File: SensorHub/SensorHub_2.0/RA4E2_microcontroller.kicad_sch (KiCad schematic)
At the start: 29 parts, among them J5 FTSH-105-01-L-DV-K-A, SW1 SW_Push, SW2 SW_Push, U1 R7FA4E2B93CFM#AA0, Y1 ASH7KW-32.768KHZ-L-T

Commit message: Fix2 17.04
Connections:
- no-connect marks 36 -> 38
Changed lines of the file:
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@@
+	)
+	(no_connect
+		(at 246.38 118.11)
 	)
 	(no_connect
@@
 	)
 	(no_connect
+		(at 246.38 115.57)
+	)
+	(no_connect

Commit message: Vesrion 2
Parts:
- removed J5: FTSH-105-01-L-DV-K-A, FTSH-105-01-L-DV-K-A:SAMTEC_FTSH-105-01-L-DV-K-A, symbol FTSH-105-01-L-DV-K-A:FTSH-105-01-L-DV-K-A
- removed R5: 1.5 K, Resistor_SMD:R_0201_0603Metric, symbol Device:R
- removed R6: 10 K, Resistor_SMD:R_0201_0603Metric, symbol Device:R
- removed SW2: SW_Push, Library:B3U-1000P(M)-B, symbol Library:SW_Push
- added J1: Conn_01x04_Pin, Connector_PinHeader_1.27mm:PinHeader_1x04_P1.27mm_Vertical, symbol Connector:Conn_01x04_Pin
- added U9: USBLC6-4SC6, Package_TO_SOT_SMD:SOT-23-6, symbol Power_Protection:USBLC6-4SC6
- TP1, TP10, TP3, TP4, TP5, TP6, TP8: footprint TestPoint:TestPoint_THTPad_D1.0mm_Drill0.5mm -> TestPoint:TestPoint_Pad_1.0x1.0mm
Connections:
- net +3.3V: now also J1.4 (Pin_4), U9.5 (VBUS)
- net GND: now also J1.3 (Pin_3), U9.2 (GND)
- net GP1: now also U1.49 (CACREF); no longer U1.14 (P409)
- net GP2: now also U1.22 (P206); no longer U1.30 (P302)
- net GP3: now also U1.21 (CACREF); no longer U1.29 (P303)
- net INT1: now also U1.51 (P006); no longer U1.1 (P400)
- net INT2: now also U1.50 (P008); no longer U1.44 (P104)
- net LED: now also U1.54 (P013); no longer U1.27 (P200)
- net RXD: now also TP8.1, U1.3 (CACREF); no longer U1.48 (P100)
- net SCL_0: now also U1.48 (P100); no longer U1.2 (P401)
- net SDA_0: now also U1.47 (P101); no longer U1.4 (P403)
- net SWCLK: now also J1.1 (Pin_1), U9.1 (I/O1)
- net SWDIO: now also J1.2 (Pin_2), U9.3 (I/O2)
- net TXD: now also U1.2 (P401); no longer TP8.1, U1.47 (P101)
- no-connect marks 38 -> 35
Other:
- note added: "Reset"
- note removed: "Reset/Boot"
- moved on the sheet: C7, R4, SW1

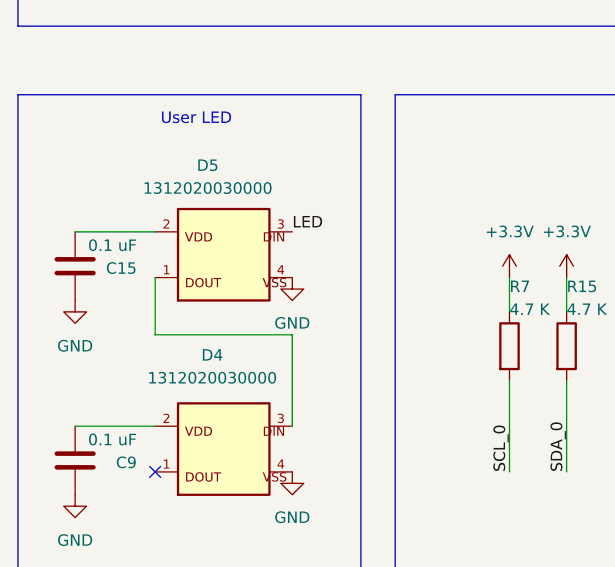
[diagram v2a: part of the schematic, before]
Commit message: MPN + CC fix
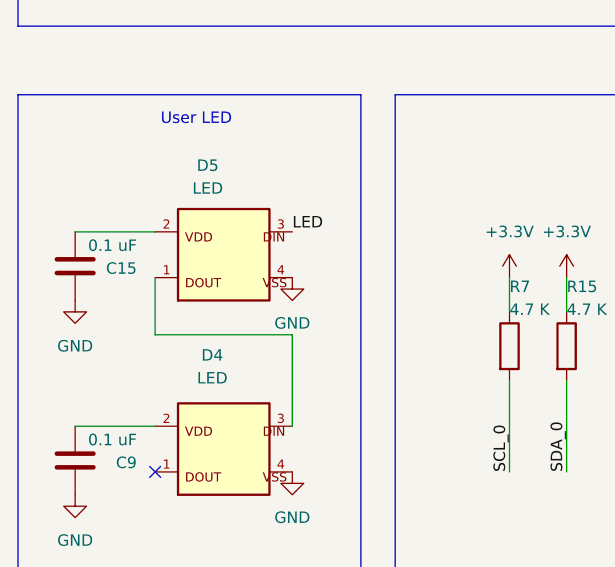
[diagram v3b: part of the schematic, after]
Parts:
- D4, D5: value 1312020030000 -> LED; MPN (none) -> 1312020030000
- SW1: MPN (none) -> B3U-1000PM-B
- U1: MPN (none) -> R7FA4E2B93CFM#AA0
- U9: MPN (none) -> USBLC6-4SC6Y
- Y1: MPN (none) -> ASH7KW-32.768KHZ-L-T
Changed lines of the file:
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@@
 			)
 		)
-		(property "Datasheet" ""
+		(property "Datasheet" "https://nl.mouser.com/datasheet/3/184/1/ASH7KW.pdf"
 			(at 54.61 93.98 0)
 			(effects
@@
 				)
 				(justify bottom)
+				(hide yes)
+			)
+		)
+		(property "MPN" "ASH7KW-32.768KHZ-L-T "
+			(at 54.61 93.98 0)
+			(effects
+				(font
+					(size 1.27 1.27)
+				)
 				(hide yes)
 			)
@@
 			)
 		)
+		(property "MPN" "R7FA4E2B93CFM#AA0"
+			(at 203.2 36.83 0)
+			(effects
+				(font
+					(size 1.27 1.27)
+				)
+				(hide yes)
+			)
+		)
 		(pin "39"
 		)
@@
 			)
 		)
-		(property "Value" "1312020030000"
+		(property "Value" "LED"
 			(at 45.212 125.984 0)
 			(effects
@@
 			)
 		)
-		(property "Datasheet" ""
+		(property "Datasheet" "https://www.we-online.com/components/products/datasheet/1312020030000.pdf"
 			(at 46.99 133.35 0)
 			(effects
@@
 				)
 				(justify bottom)
+				(hide yes)
+			)
+		)
+		(property "MPN" "1312020030000"
+			(at 46.99 133.35 0)
+			(effects
+				(font
+					(size 1.27 1.27)
+				)
 				(hide yes)
 			)
@@
 			)
 		)
-		(property "Datasheet" "~"
+		(property "Datasheet" "https://www.mouser.com/catalog/specsheets/en-b3u.pdf?_gl=1*1hale0w*_gcl_aw*R0NMLjE3Nzc1NDczODcuQ2p3S0NBanctOHZQQmhCYkVpd0FvQTM5V21qOE1FMEhGMTJsZnVsd1dsanpUT2lLOUp5a3NWMndHOXk0X2pxV0NTQ1ZHQTdyREplemFSb0NiajRRQXZEX0J3RQ..*_gcl_au*MTEyMDA2MzkwNS4xNzczNDExMzc2LjMyODU5NDQyNi4xNzc3NTQ2NjQ1LjE3Nzc1NDg3NTQ.*_ga*Mjg1MTQ4MTY2LjE3NzM0MTEzNzc.*_ga_15W4STQT4T*czE3Nzc1NDUwNzgkbzU0JGcxJHQxNzc3NTQ4NzU4JGozJGwwJGgw"
 			(at 139.7 57.15 0)
 			(effects
@@
 		(property "Description" "Push button switch, generic, two pins"
 			(at 144.78 57.15 0)
+			(effects
+				(font
+					(size 1.27 1.27)
+				)
+				(hide yes)
+			)
+		)
+		(property "MPN" "B3U-1000PM-B"
+			(at 144.78 57.15 90)
 			(effects
 				(font
@@
 			)
 		)
+		(property "MPN" "USBLC6-4SC6Y "
+			(at 82.55 50.8 0)
+			(effects
+				(font
+					(size 1.27 1.27)
+				)
+				(hide yes)
+			)
+		)
 		(pin "6"
 		)
@@
 			)
 		)
-		(property "Value" "1312020030000"
+		(property "Value" "LED"
 			(at 45.72 147.066 0)
 			(effects
@@
 			)
 		)
-		(property "Datasheet" ""
+		(property "Datasheet" "https://www.we-online.com/components/products/datasheet/1312020030000.pdf"
 			(at 46.99 154.94 0)
 			(effects
@@
 				(hide yes)
 			)
+		)
+		(property "MPN" "1312020030000"
+			(at 46.99 154.94 0)
+			(effects
+				(font
+					(size 1.27 1.27)
+				)
+				(hide yes)
+			)

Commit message: pcb fix
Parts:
- added R17, R18: 4.7 K, Resistor_SMD:R_0402_1005Metric, symbol Device:R
- R15, R4, R7: footprint Resistor_SMD:R_0201_0603Metric -> Resistor_SMD:R_0402_1005Metric
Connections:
- net USB_DM: now also R18.2; no longer U1.18 (USB_DM)
- net USB_DP: now also R17.2; no longer U1.19 (USB_DP)
- new net DM: R18.1, U1.18 (USB_DM)
- new net DP: R17.1, U1.19 (USB_DP)
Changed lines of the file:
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@@
 	)
 	(rectangle
+		(start 114.3 148.59)
+		(end 137.16 189.23)
+		(stroke
+			(width 0)
+			(type default)
+		)
+		(fill
+			(type none)
+		)
+	)
+	(rectangle
 		(start 66.04 115.57)
 		(end 97.79 170.18)
@@
 	(wire
 		(pts
+			(xy 121.92 177.8) (xy 121.92 171.45)
+		)
+		(stroke
+			(width 0)
+			(type default)
+		)
+	)
+	(wire
+		(pts
 			(xy 137.16 66.04) (xy 144.78 66.04)
 		)
@@
 	(wire
 		(pts
+			(xy 128.27 163.83) (xy 128.27 156.21)
+		)
+		(stroke
+			(width 0)
+			(type default)
+		)
+	)
+	(wire
+		(pts
 			(xy 138.43 123.19) (xy 138.43 115.57)
 		)
@@
 	(wire
 		(pts
+			(xy 128.27 177.8) (xy 128.27 171.45)
+		)
+		(stroke
+			(width 0)
+			(type default)
+		)
+	)
+	(wire
+		(pts
 			(xy 133.35 49.53) (xy 137.16 49.53)
 		)
@@
 	(wire
 		(pts
+			(xy 121.92 156.21) (xy 121.92 163.83)
+		)
+		(stroke
+			(width 0)
+			(type default)
+		)
+	)
+	(wire
+		(pts
 			(xy 161.29 115.57) (xy 161.29 123.19)
 		)
@@
 		)
 	)
+	(label "DM"
+		(at 205.74 87.63 180)
+		(effects
+			(font
+				(size 1.27 1.27)
+			)
+			(justify right bottom)
+		)
+	)
 	(label "+3.3V"
 		(at 153.67 99.06 180)
@@
 		)
 	)
+	(label "DP"
+		(at 205.74 85.09 180)
+		(effects
+			(font
+				(size 1.27 1.27)
+			)
+			(justify right bottom)
+		)
+	)
 	(label "SWCLK"
 		(at 205.74 95.25 180)
@@
 		)
 	)
+	(label "DP"
+		(at 121.92 156.21 90)
+		(effects
+			(font
+				(size 1.27 1.27)
+			)
+			(justify left bottom)
+		)
+	)
 	(label "SWCLK"
 		(at 60.96 49.53 0)
@@
 		)
 	)
+	(label "DM"
+		(at 128.27 156.21 90)
+		(effects
+			(font
+				(size 1.27 1.27)
+			)
+			(justify left bottom)
+		)
+	)
 	(hierarchical_label "MOSI"
 		(shape input)
@@
 		)
 	)
+	(hierarchical_label "USB_DP"
+		(shape input)
+		(at 121.92 177.8 270)
+		(effects
+			(font
+				(size 1.27 1.27)
+			)
+			(justify right)
+		)
+	)
 	(hierarchical_label "SCK"
 		(shape input)
@@
 		)
 	)
-	(hierarchical_label "SDA_0"
+	(hierarchical_label "USB_DM"
 		(shape input)
-		(at 246.38 46.99 0)
+		(at 128.27 177.8 270)
 		(effects
 			(font
 				(size 1.27 1.27)
 			)
-			(justify left)
+			(justify right)
 		)
 	)
-	(hierarchical_label "INT1"
+	(hierarchical_label "SDA_0"
 		(shape input)
-		(at 205.74 130.81 180)
+		(at 246.38 46.99 0)
 		(effects
 			(font
 				(size 1.27 1.27)
 			)
-			(justify right)
+			(justify left)
 		)
 	)
-	(hierarchical_label "USB_DP"
+	(hierarchical_label "INT1"
 		(shape input)
-		(at 205.74 85.09 180)
+		(at 205.74 130.81 180)
 		(effects
 			(font
@@
 		)
 	)
-	(hierarchical_label "USB_DM"
-		(shape input)
-		(at 205.74 87.63 180)
-		(effects
-			(font
-				(size 1.27 1.27)
-			)
-			(justify right)
-		)
-	)
 	(hierarchical_label "RXD"
 		(shape input)
@@
 			)
 		)
-		(property "Footprint" "Resistor_SMD:R_0201_0603Metric"
+		(property "Footprint" "Resistor_SMD:R_0402_1005Metric"
 			(at 76.962 143.51 90)
 			(effects
@@
 			)
 		)
-		(property "Footprint" "Resistor_SMD:R_0201_0603Metric"
+		(property "Footprint" "Resistor_SMD:R_0402_1005Metric"
 			(at 143.002 44.45 90)
 			(effects
@@
 	)
 	(symbol
+		(lib_id "Device:R")
+		(at 121.92 167.64 0)
+		(unit 1)
+		(exclude_from_sim no)
+		(in_bom yes)
+		(on_board yes)
+		(dnp no)
+		(property "Reference" "R17"
+			(at 121.92 161.036 0)
+			(effects
+				(font
+					(size 1.27 1.27)
+				)
+				(justify left)
+			)
+		)
+		(property "Value" "4.7 K"
+			(at 121.92 163.576 0)
+			(effects
+				(font
+					(size 1.27 1.27)
+				)
+				(justify left)
+			)
+		)
+		(property "Footprint" "Resistor_SMD:R_0402_1005Metric"
+			(at 120.142 167.64 90)
+			(effects
+				(font
+					(size 1.27 1.27)
+				)
+				(hide yes)
+			)
+		)
+		(property "Datasheet" "~"
+			(at 121.92 167.64 0)
+			(effects
+				(font
+					(size 1.27 1.27)
+				)
+				(hide yes)
+			)
+		)
+		(property "Description" "Resistor"
+			(at 121.92 167.64 0)
+			(effects
+				(font
+					(size 1.27 1.27)
+				)
+				(hide yes)
+			)
+		)
+		(pin "1"
+		)
+		(pin "2"
+		)
+		(instances
+			(project "SensorHub_2.0"
+				(path "/9668bc71-8924-498e-982f-628f3083c8b8/654fedd9-e4dd-4bc9-b3a7-f679d72db815"
+					(reference "R17")
+					(unit 1)
+				)
+			)
+		)
+	)
+	(symbol
 		(lib_id "power:GND")
 		(at 144.78 71.12 0)
@@
 			)
 		)
-		(property "Footprint" "Resistor_SMD:R_0201_0603Metric"
+		(property "Footprint" "Resistor_SMD:R_0402_1005Metric"
 			(at 83.312 143.51 90)
 			(effects
@@
 					(unit 1)
 				)
+			)
+		)
+	)
+	(symbol
+		(lib_id "Device:R")
+		(at 128.27 167.64 0)
+		(unit 1)
+		(exclude_from_sim no)
+		(in_bom yes)
+		(on_board yes)
+		(dnp no)
+		(property "Reference" "R18"
+			(at 128.27 161.036 0)
+			(effects
+				(font
+					(size 1.27 1.27)
+				)
+				(justify left)
+			)
+		)
+		(property "Value" "4.7 K"
+			(at 128.27 163.576 0)
+			(effects
+				(font
+					(size 1.27 1.27)
+				)
+				(justify left)
+			)
+		)
+		(property "Footprint" "Resistor_SMD:R_0402_1005Metric"
+			(at 126.492 167.64 90)
+			(effects
+				(font
+					(size 1.27 1.27)
+				)
+				(hide yes)
+			)
+		)
+		(property "Datasheet" "~"
+			(at 128.27 167.64 0)
+			(effects
+				(font
+					(size 1.27 1.27)
+				)
+				(hide yes)
+			)
+		)
+		(property "Description" "Resistor"
+			(at 128.27 167.64 0)
+			(effects
+				(font
+					(size 1.27 1.27)
+				)
+				(hide yes)
+			)
+		)
+		(pin "1"
+		)
+		(pin "2"
+		)
+		(instances
+			(project "SensorHub_2.0"
+				(path "/9668bc71-8924-498e-982f-628f3083c8b8/654fedd9-e4dd-4bc9-b3a7-f679d72db815"
+					(reference "R18")
+					(unit 1)
+				)

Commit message: DP/DM
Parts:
- removed TP6: TestPoint, TestPoint:TestPoint_Pad_1.0x1.0mm, symbol Connector:TestPoint
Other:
- moved on the sheet: TP10, TP8
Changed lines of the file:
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@@
 	)
 	(label "RXD"
-		(at 43.18 43.18 0)
+		(at 41.91 46.99 0)
 		(effects
 			(font
@@
 		)
 	)
-	(label "EXTAL"
-		(at 41.91 46.99 0)
-		(effects
-			(font
-				(size 1.27 1.27)
-			)
-			(justify left bottom)
-		)
-	)
 	(label "LED"
 		(at 205.74 135.89 180)
@@
 	)
 	(label "GND"
-		(at 40.64 40.64 0)
+		(at 43.18 43.18 0)
 		(effects
 			(font
@@
 	(symbol
 		(lib_id "Connector:TestPoint")
-		(at 43.18 43.18 90)
-		(unit 1)
-		(exclude_from_sim no)
-		(in_bom yes)
-		(on_board yes)
-		(dnp no)
-		(property "Reference" "TP8"
-			(at 34.798 47.752 0)
-			(effects
-				(font
-					(size 1.27 1.27)
-				)
-				(justify left)
-			)
-		)
-		(property "Value" "TestPoint"
-			(at 36.3219 47.752 0)
-			(effects
-				(font
-					(size 1.27 1.27)
-				)
-				(justify left)
-				(hide yes)
-			)
-		)
-		(property "Footprint" "TestPoint:TestPoint_Pad_1.0x1.0mm"
-			(at 43.18 38.1 0)
-			(effects
-				(font
-					(size 1.27 1.27)
-				)
-				(hide yes)
-			)
-		)
-		(property "Datasheet" "~"
-			(at 43.18 38.1 0)
-			(effects
-				(font
-					(size 1.27 1.27)
-				)
-				(hide yes)
-			)
-		)
-		(property "Description" "test point"
-			(at 43.18 43.18 0)
-			(effects
-				(font
-					(size 1.27 1.27)
-				)
-				(hide yes)
-			)
-		)
-		(pin "1"
-		)
-		(instances
-			(project "SensorHub_2.0"
-				(path "/9668bc71-8924-498e-982f-628f3083c8b8/654fedd9-e4dd-4bc9-b3a7-f679d72db815"
-					(reference "TP8")
-					(unit 1)
-				)
-			)
-		)
-	)
-	(symbol
-		(lib_id "Connector:TestPoint")
 		(at 41.91 46.99 90)
 		(unit 1)
@@
 		(on_board yes)
 		(dnp no)
-		(property "Reference" "TP6"
+		(property "Reference" "TP8"
 			(at 33.528 51.562 0)
 			(effects
@@
 			(project "SensorHub_2.0"
 				(path "/9668bc71-8924-498e-982f-628f3083c8b8/654fedd9-e4dd-4bc9-b3a7-f679d72db815"
-					(reference "TP6")
+					(reference "TP8")
 					(unit 1)
 				)
@@
 	(symbol
 		(lib_id "Connector:TestPoint")
-		(at 40.64 40.64 90)
+		(at 43.18 43.18 90)
 		(unit 1)
 		(exclude_from_sim no)
@@
 		(dnp no)
 		(property "Reference" "TP10"
-			(at 32.258 45.212 0)
+			(at 34.798 47.752 0)
 			(effects
 				(font
@@
 		)
 		(property "Value" "TestPoint"
-			(at 33.7819 45.212 0)
+			(at 36.3219 47.752 0)
 			(effects
 				(font
@@
 		)
 		(property "Footprint" "TestPoint:TestPoint_Pad_1.0x1.0mm"
-			(at 40.64 35.56 0)
+			(at 43.18 38.1 0)
 			(effects
 				(font
@@
 		)
 		(property "Datasheet" "~"
-			(at 40.64 35.56 0)
+			(at 43.18 38.1 0)
 			(effects
 				(font
@@
 		)
 		(property "Description" "test point"
-			(at 40.64 40.64 0)
+			(at 43.18 43.18 0)
 			(effects
 				(font

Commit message: v 2.3
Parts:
- R15, R17, R18, R4, R7: footprint Resistor_SMD:R_0402_1005Metric -> Resistor_SMD:R_0603_1608Metric
- Y1: footprint ASH7KW-32.768KHZ-L-T:XTAL_ASH7KW-32.768KHZ-L-T -> XTAL_ASH7KW-32.768KHZ-L-T:XTAL_ASH7KW-32.768KHZ-L-T
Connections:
- net GP2: now also U1.54 (P013); no longer U1.22 (P206)
- net GP3: now also U1.55 (P003); no longer U1.21 (CACREF)
- net LED: now also U1.60 (P005); no longer U1.54 (P013)
- net SWCLK: now also U9.3 (I/O2); no longer U9.1 (I/O1)
- net SWDIO: now also U9.1 (I/O1); no longer U9.3 (I/O2)
